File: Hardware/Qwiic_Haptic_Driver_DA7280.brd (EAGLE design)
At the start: 25.4 x 25.4 mm, 48 parts, among them J1 QWIIC_RIGHT_ANGLE, J2 QWIIC_RIGHT_ANGLE, M1 G1040003D_LRA_CASTELLATED, U1 HAPTIC_DRIVER_DA7280

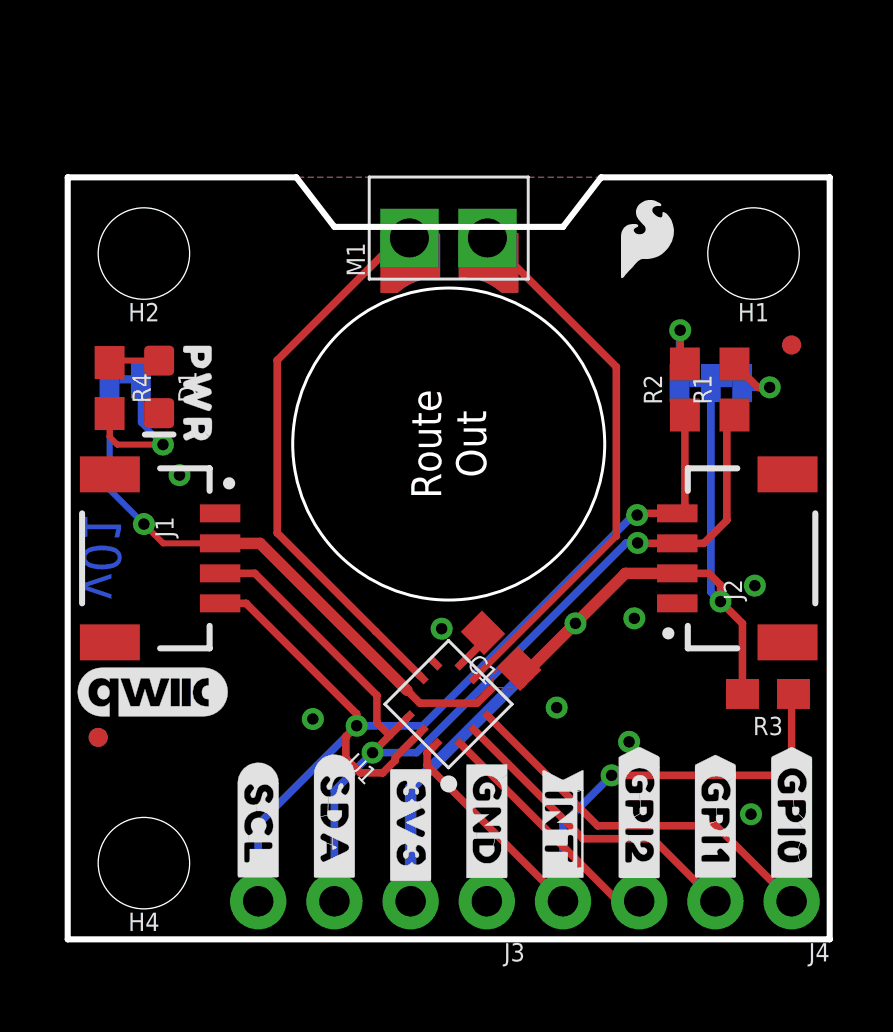
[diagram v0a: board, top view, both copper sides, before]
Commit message: Flips the LRA motor 180, extends board to be 1.15 x 1 inches, adds 4.7iF decoupling capacitor
* Gerbers in repo are out of date
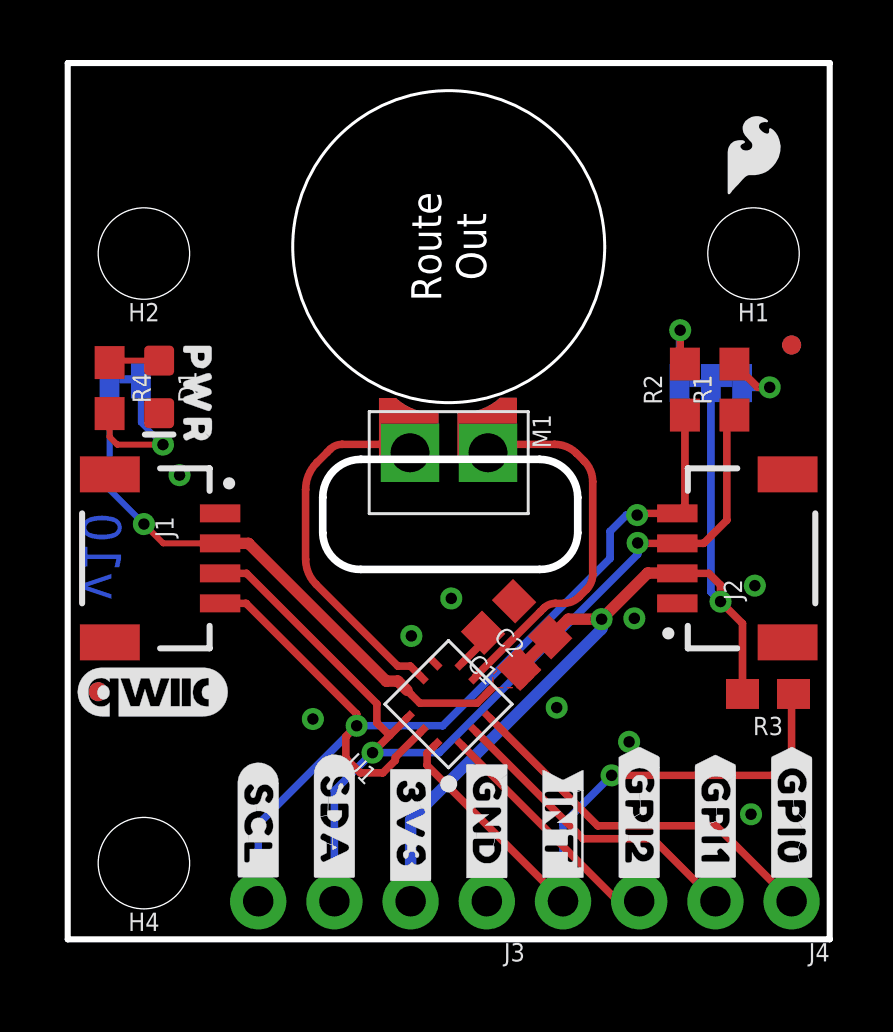
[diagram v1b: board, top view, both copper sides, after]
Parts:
- added C2: 4.7uF, SparkFun-Capacitors:0603
- moved M1 6.58 mm to (12.7, 23.1), turned to 270 degrees
- moved U$22 4.58 mm to (2.43, 25.8)
- moved U$17 4.52 mm to (22.9, 26.2)
- moved U$26 4.52 mm to (22.7, 26.2)
- moved FD1 1.52 mm to (1.02, 8.26)
- moved FD2 1.52 mm to (1.02, 8.26)
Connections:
- net 3.3V: now also C2.1
- net GND: now also C2.2
- net N$5: now also U1.P5; no longer U1.P8
- net N$6: now also U1.P8; no longer U1.P5
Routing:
- net N$5: track 18.6 -> 12.7 mm
- net N$6: track 18.3 -> 12.4 mm
- net 3.3V: track 50.6 -> 51.1 mm
- net SCL: track 35.2 -> 35.8 mm
- net GND: vias 8 -> 9
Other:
- board size 25.4 x 25.4 mm -> 25.4 x 29.2 mm
- board text added: "v10"
- board text removed: "v01"

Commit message: Widens the power traces to .02" , rotates the GND,VCC, SDA, SCL header
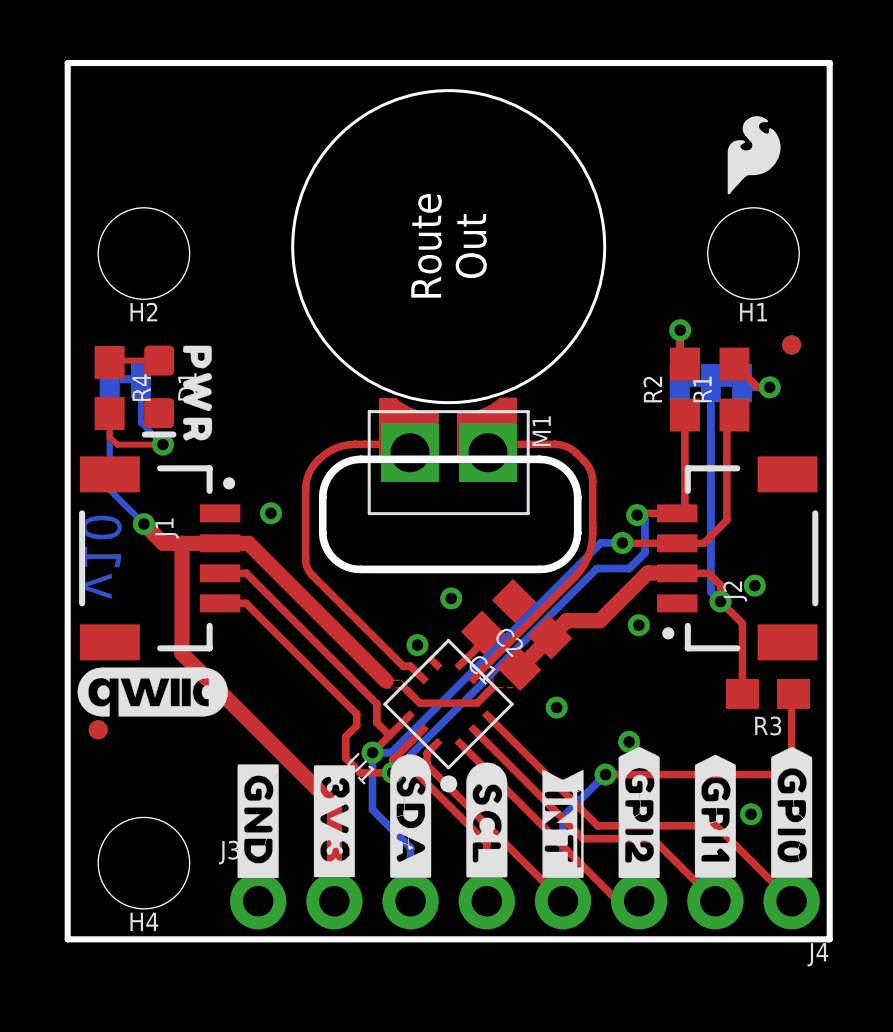
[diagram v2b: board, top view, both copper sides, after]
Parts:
- moved J3 7.62 mm to (6.35, 1.27), turned to 0 degrees
- moved U$18 7.62 mm to (6.35, 3.94)
- moved U$19 7.62 mm to (14.0, 3.81)
- moved U$21 7.62 mm to (14.0, 3.81)
- moved U$3 7.62 mm to (6.35, 3.94)
- moved U$2 2.54 mm to (8.89, 3.94)
- moved U$25 2.54 mm to (8.89, 3.94)
- moved U$16 2.54 mm to (11.4, 3.94)
- moved U$8 2.54 mm to (11.4, 3.94)
- moved FD1 1.27 mm to (1.02, 6.99)
- moved FD2 1.27 mm to (1.02, 6.99)
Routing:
- net 3.3V: track 51.1 -> 52.3 mm, vias 3 -> 2
- net SCL: track 35.8 -> 34.9 mm
- net GND: vias 9 -> 8
